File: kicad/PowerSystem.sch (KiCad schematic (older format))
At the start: 15 parts, among them U201 LF120ABDT-TR, U202 TPS70933

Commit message: Started assigning foot prints to the parts
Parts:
- removed W201: TEST_1P, symbol TEST_1P
- C201: footprint (none) -> Capacitors_SMD:C_0805
- C202: value 1μF 50V -> 1μF 25V; footprint (none) -> Capacitors_SMD:C_1210; Conrad-PN (none) -> Value; Digikey-PN (none) -> Value; MFP (none) -> Value
- C203: value 02.2μF 50V -> 2.2μF 50V; footprint (none) -> Capacitors_SMD:C_1210; Conrad-PN (none) -> N/A; Digikey-PN (none) -> 1276-2884-1-ND; MFP (none) -> CL32B225KBJNNNE
- C204: footprint (none) -> Capacitors_SMD:C_1210; Conrad-PN (none) -> Value; Digikey-PN (none) -> Value; MFP (none) -> Value
- D201: value LED -> 12VDC; footprint (none) -> LEDs:LED_0805
- D202: value LED -> 3V3DC; footprint (none) -> LEDs:LED_0805
- R201, R202, R203, R204: footprint (none) -> Resistors_SMD:R_0805
- TP201, TP202: footprint (none) -> Measurement_Points:Measurement_Point_Round-SMD-Pad_Small
- U201: Conrad-PN (none) -> 1185937 - 62; Digikey-PN (none) -> 497-8330-1-ND
- U202: Conrad-PN (none) -> 1261694 - 62; Digikey-PN (none) -> 296-35483-1-ND
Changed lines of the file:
@@
 F 0 "R202" V 3280 3850 50  0000 C CNN
 F 1 "0Ω" V 3200 3850 50  0000 C CNN
-F 2 "" V 3130 3850 50  0000 C CNN
+F 2 "Resistors_SMD:R_0805" V 3130 3850 50  0001 C CNN
 F 3 "" H 3200 3850 50  0000 C CNN
 	1    3200 3850
@@
 U+
 $Comp
-L GND #PWR202
+L GND #PWR011
 U 1 1 584DB061
 P 3900 4450
-F 0 "#PWR202" H 3900 4200 50  0001 C CNN
+F 0 "#PWR011" H 3900 4200 50  0001 C CNN
 F 1 "GND" H 3900 4300 50  0000 C CNN
 F 2 "" H 3900 4450 50  0000 C CNN
@@
 P 2600 4050
 F 0 "C202" H 2625 4150 50  0000 L CNN
-F 1 "1μF 50V" H 2625 3950 50  0000 L CNN
-F 2 "" H 2638 3900 50  0000 C CNN
+F 1 "1μF 25V" H 2625 3950 50  0000 L CNN
+F 2 "Capacitors_SMD:C_1210" H 2638 3900 50  0001 C CNN
 F 3 "" H 2600 4050 50  0000 C CNN
+F 4 "Value" H 2600 4050 60  0001 C CNN "MFP"
+F 5 "Value" H 2600 4050 60  0001 C CNN "Conrad-PN"
+F 6 "Value" H 2600 4050 60  0001 C CNN "Digikey-PN"
 	1    2600 4050
 	1    0    0    -1
@@
 F 0 "C204" H 4675 4150 50  0000 L CNN
 F 1 "1μF 16V" H 4675 3950 50  0000 L CNN
-F 2 "" H 4688 3900 50  0000 C CNN
+F 2 "Capacitors_SMD:C_1210" H 4688 3900 50  0001 C CNN
 F 3 "" H 4650 4050 50  0000 C CNN
+F 4 "Value" H 4650 4050 60  0001 C CNN "MFP"
+F 5 "Value" H 4650 4050 60  0001 C CNN "Conrad-PN"
+F 6 "Value" H 4650 4050 60  0001 C CNN "Digikey-PN"
 	1    4650 4050
 	1    0    0    -1
@@
 P 5250 4050
 F 0 "D202" H 5250 4150 50  0000 C CNN
-F 1 "LED" H 5250 3950 50  0000 C CNN
-F 2 "" H 5250 4050 50  0000 C CNN
+F 1 "3V3DC" H 5250 3950 50  0000 C CNN
+F 2 "LEDs:LED_0805" H 5250 4050 50  0001 C CNN
 F 3 "" H 5250 4050 50  0000 C CNN
 	1    5250 4050
@@
 F 0 "R204" V 5330 4550 50  0000 C CNN
 F 1 "660Ω" V 5250 4550 50  0000 C CNN
-F 2 "" V 5180 4550 50  0000 C CNN
+F 2 "Resistors_SMD:R_0805" V 5180 4550 50  0001 C CNN
 F 3 "" H 5250 4550 50  0000 C CNN
 	1    5250 4550
@@
 $EndComp
 $Comp
-L GND #PWR204
+L GND #PWR012
 U 1 1 584DB084
 P 5250 4900
-F 0 "#PWR204" H 5250 4650 50  0001 C CNN
+F 0 "#PWR012" H 5250 4650 50  0001 C CNN
 F 1 "GND" H 5250 4750 50  0000 C CNN
 F 2 "" H 5250 4900 50  0000 C CNN
 F 3 "" H 5250 4900 50  0000 C CNN
 	1    5250 4900
-	1    0    0    -1
-$EndComp
-$Comp
-L TEST_1P W201
-U 1 1 584DB091
-P 2500 3500
-F 0 "W201" H 2500 3770 50  0000 C CNN
-F 1 "TEST_1P" H 2500 3700 50  0000 C CNN
-F 2 "" H 2700 3500 50  0000 C CNN
-F 3 "" H 2700 3500 50  0000 C CNN
-	1    2500 3500
 	1    0    0    -1
 $EndComp
@@
 F 0 "U202" H 4150 3350 60  0000 C CNN
 F 1 "TPS70933" H 3900 3700 60  0000 C CNN
-F 2 "" H 3750 3700 60  0000 C CNN
+F 2 "" H 3750 3700 60  0001 C CNN
 F 3 "" H 3750 3700 60  0000 C CNN
 F 4 "TPS70933DBVR" H 3900 3700 60  0001 C CNN "MFP"
+F 5 "1261694 - 62" H 3900 3700 60  0001 C CNN "Conrad-PN"
+F 6 "296-35483-1-ND" H 3900 3700 60  0001 C CNN "Digikey-PN"
 	1    3900 3700
 	1    0    0    -1
@@
 F 0 "U201" H 4150 1200 60  0000 C CNN
 F 1 "LF120ABDT-TR" H 3900 1550 60  0000 C CNN
-F 2 "" H 3750 1550 60  0000 C CNN
+F 2 "" H 3750 1550 60  0001 C CNN
 F 3 "" H 3750 1550 60  0000 C CNN
 F 4 "LF120ABDT-TR" H 3900 1550 60  0001 C CNN "MFP"
+F 5 "1185937 - 62" H 3900 1550 60  0001 C CNN "Conrad-PN"
+F 6 "497-8330-1-ND" H 3900 1550 60  0001 C CNN "Digikey-PN"
 	1    3900 1550
 	1    0    0    -1
@@
 	5400 3500 5400 3550
 Connection ~ 5400 3550
-Wire Wire Line
-	2500 3500 2500 3550
-Connection ~ 2500 3550
 Text HLabel 5850 3550 2    60   Input ~ 0
 UbOut
@@
 F 0 "C201" H 2575 1950 50  0000 L CNN
 F 1 "0.1μF 50V" H 2575 1750 50  0000 L CNN
-F 2 "" H 2588 1700 50  0000 C CNN
+F 2 "Capacitors_SMD:C_0805" H 2588 1700 50  0001 C CNN
 F 3 "" H 2550 1850 50  0000 C CNN
 	1    2550 1850
@@
 P 4600 1850
 F 0 "C203" H 4625 1950 50  0000 L CNN
-F 1 "02.2μF 50V" H 4625 1750 50  0000 L CNN
-F 2 "" H 4638 1700 50  0000 C CNN
+F 1 "2.2μF 50V" H 4625 1750 50  0000 L CNN
+F 2 "Capacitors_SMD:C_1210" H 4638 1700 50  0001 C CNN
 F 3 "" H 4600 1850 50  0000 C CNN
+F 4 "CL32B225KBJNNNE" H 4600 1850 60  0001 C CNN "MFP"
+F 5 "N/A" H 4600 1850 60  0001 C CNN "Conrad-PN"
+F 6 "1276-2884-1-ND" H 4600 1850 60  0001 C CNN "Digikey-PN"
 	1    4600 1850
 	1    0    0    -1
 $EndComp
 $Comp
-L GND #PWR201
+L GND #PWR013
 U 1 1 584DD17A
 P 3900 2650
-F 0 "#PWR201" H 3900 2400 50  0001 C CNN
+F 0 "#PWR013" H 3900 2400 50  0001 C CNN
 F 1 "GND" H 3900 2500 50  0000 C CNN
 F 2 "" H 3900 2650 50  0000 C CNN
@@
 F 0 "R201" V 3280 2050 50  0000 C CNN
 F 1 "0Ω" V 3200 2050 50  0000 C CNN
-F 2 "" V 3130 2050 50  0000 C CNN
+F 2 "Resistors_SMD:R_0805" V 3130 2050 50  0001 C CNN
 F 3 "" H 3200 2050 50  0000 C CNN
 F 4 "VALUE" H 3200 2050 60  0001 C CNN "MFP"
@@
 P 5250 1850
 F 0 "D201" H 5250 1950 50  0000 C CNN
-F 1 "LED" H 5250 1750 50  0000 C CNN
-F 2 "" H 5250 1850 50  0000 C CNN
+F 1 "12VDC" H 5250 1750 50  0000 C CNN
+F 2 "LEDs:LED_0805" H 5250 1850 50  0001 C CNN
 F 3 "" H 5250 1850 50  0000 C CNN
 	1    5250 1850
@@
 F 0 "R203" V 5330 2350 50  0000 C CNN
 F 1 "2k4Ω" V 5250 2350 50  0000 C CNN
-F 2 "" V 5180 2350 50  0000 C CNN
+F 2 "Resistors_SMD:R_0805" V 5180 2350 50  0001 C CNN
 F 3 "" H 5250 2350 50  0000 C CNN
 	1    5250 2350
@@
 $EndComp
 $Comp
-L GND #PWR203
+L GND #PWR014
 U 1 1 584DD971
 P 5250 2650
-F 0 "#PWR203" H 5250 2400 50  0001 C CNN
+F 0 "#PWR014" H 5250 2400 50  0001 C CNN
 F 1 "GND" H 5250 2500 50  0000 C CNN
 F 2 "" H 5250 2650 50  0000 C CNN
@@
 F 0 "TP202" H 5600 1470 50  0000 C CNN
 F 1 "TP12V" H 5600 1400 50  0000 C CNN
-F 2 "" H 5800 1200 50  0000 C CNN
+F 2 "Measurement_Points:Measurement_Point_Round-SMD-Pad_Small" H 5800 1200 50  0001 C CNN
 F 3 "" H 5800 1200 50  0000 C CNN
 	1    5600 1200
@@
 F 0 "TP201" H 5400 3770 50  0000 C CNN
 F 1 "TP3V3" H 5400 3700 50  0000 C CNN
-F 2 "" H 5600 3500 50  0000 C CNN
+F 2 "Measurement_Points:Measurement_Point_Round-SMD-Pad_Small" H 5600 3500 50  0001 C CNN
 F 3 "" H 5600 3500 50  0000 C CNN
 	1    5400 3500

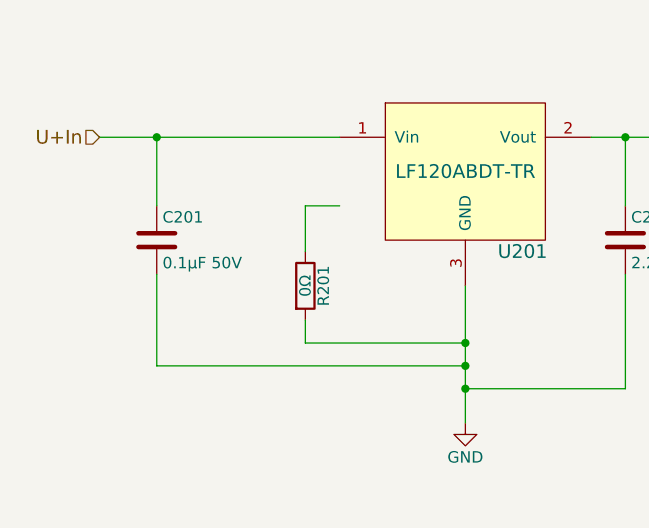
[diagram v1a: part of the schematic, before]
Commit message: Added more footprints to the parts
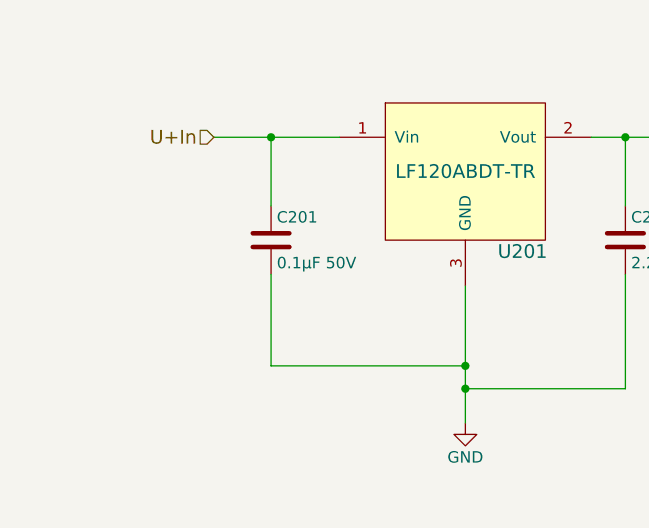
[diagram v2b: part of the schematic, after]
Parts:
- removed R201: 0Ω, Resistors_SMD:R_0805, symbol R
- U201: footprint (none) -> tl2c-footprint:LF120ABDT-TR
- U202: footprint (none) -> tl2c-footprint:TPS70933DBVR
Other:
- moved on the sheet: C201
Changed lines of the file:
@@
 F 0 "U202" H 4150 3350 60  0000 C CNN
 F 1 "TPS70933" H 3900 3700 60  0000 C CNN
-F 2 "" H 3750 3700 60  0001 C CNN
+F 2 "tl2c-footprint:TPS70933DBVR" H 3750 3700 60  0001 C CNN
 F 3 "" H 3750 3700 60  0000 C CNN
 F 4 "TPS70933DBVR" H 3900 3700 60  0001 C CNN "MFP"
@@
 F 0 "U201" H 4150 1200 60  0000 C CNN
 F 1 "LF120ABDT-TR" H 3900 1550 60  0000 C CNN
-F 2 "" H 3750 1550 60  0001 C CNN
+F 2 "tl2c-footprint:LF120ABDT-TR" H 3750 1550 60  0001 C CNN
 F 3 "" H 3750 1550 60  0000 C CNN
 F 4 "LF120ABDT-TR" H 3900 1550 60  0001 C CNN "MFP"
@@
 	4450 1400 6150 1400
 Wire Wire Line
-	2300 1400 3350 1400
+	2800 1400 3350 1400
 $Comp
 L C C201
 U 1 1 584DCFF9
-P 2550 1850
-F 0 "C201" H 2575 1950 50  0000 L CNN
-F 1 "0.1μF 50V" H 2575 1750 50  0000 L CNN
-F 2 "Capacitors_SMD:C_0805" H 2588 1700 50  0001 C CNN
-F 3 "" H 2550 1850 50  0000 C CNN
-	1    2550 1850
+P 3050 1850
+F 0 "C201" H 3075 1950 50  0000 L CNN
+F 1 "0.1μF 50V" H 3075 1750 50  0000 L CNN
+F 2 "Capacitors_SMD:C_0805" H 3088 1700 50  0001 C CNN
+F 3 "" H 3050 1850 50  0000 C CNN
+	1    3050 1850
 	1    0    0    -1
 $EndComp
@@
 Text HLabel 6150 1400 2    60   Input ~ 0
 U+Out
-Text HLabel 2300 1400 0    60   Input ~ 0
+Text HLabel 2800 1400 0    60   Input ~ 0
 U+In
 Wire Wire Line
 	3900 2050 3900 2650
-$Comp
-L R R201
-U 1 1 584DD244
-P 3200 2050
-F 0 "R201" V 3280 2050 50  0000 C CNN
-F 1 "0Ω" V 3200 2050 50  0000 C CNN
-F 2 "Resistors_SMD:R_0805" V 3130 2050 50  0001 C CNN
-F 3 "" H 3200 2050 50  0000 C CNN
-F 4 "VALUE" H 3200 2050 60  0001 C CNN "MFP"
-	1    3200 2050
-	1    0    0    -1
-$EndComp
 Wire Wire Line
-	3350 1700 3200 1700
+	3050 1400 3050 1700
+Connection ~ 3050 1400
 Wire Wire Line
-	3200 1700 3200 1900
+	3050 2000 3050 2400
 Wire Wire Line
-	3200 2200 3200 2300
-Wire Wire Line
-	3200 2300 3900 2300
-Connection ~ 3900 2300
-Wire Wire Line
-	2550 1400 2550 1700
-Connection ~ 2550 1400
-Wire Wire Line
-	2550 2000 2550 2400
-Wire Wire Line
-	2550 2400 3900 2400
+	3050 2400 3900 2400
 Connection ~ 3900 2400
 Wire Wire Line

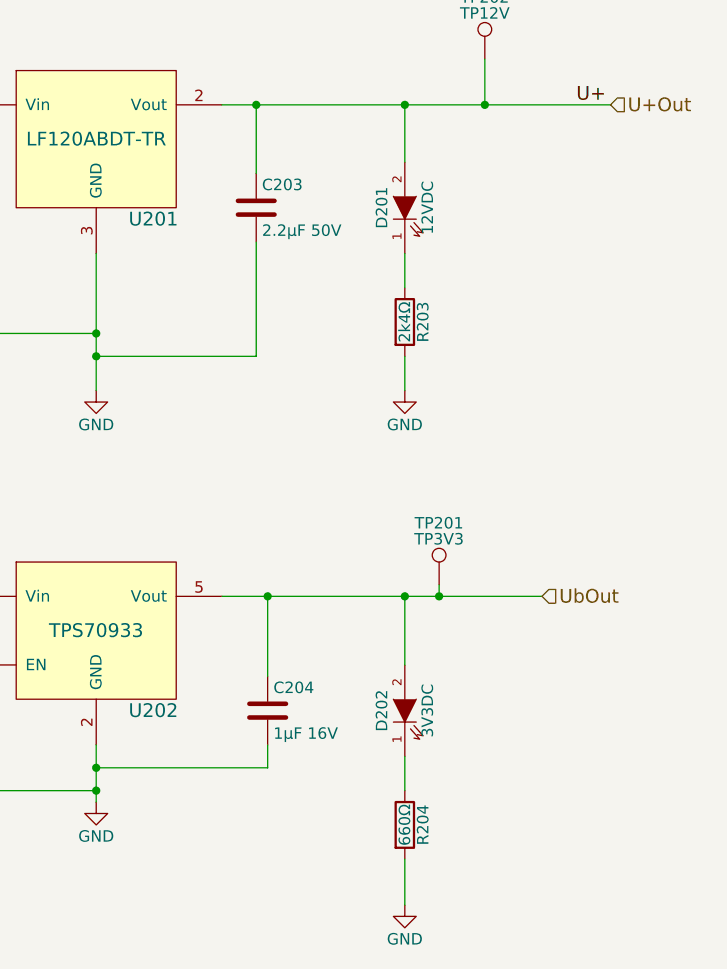
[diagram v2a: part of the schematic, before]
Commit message: Started adding tracks to the layout
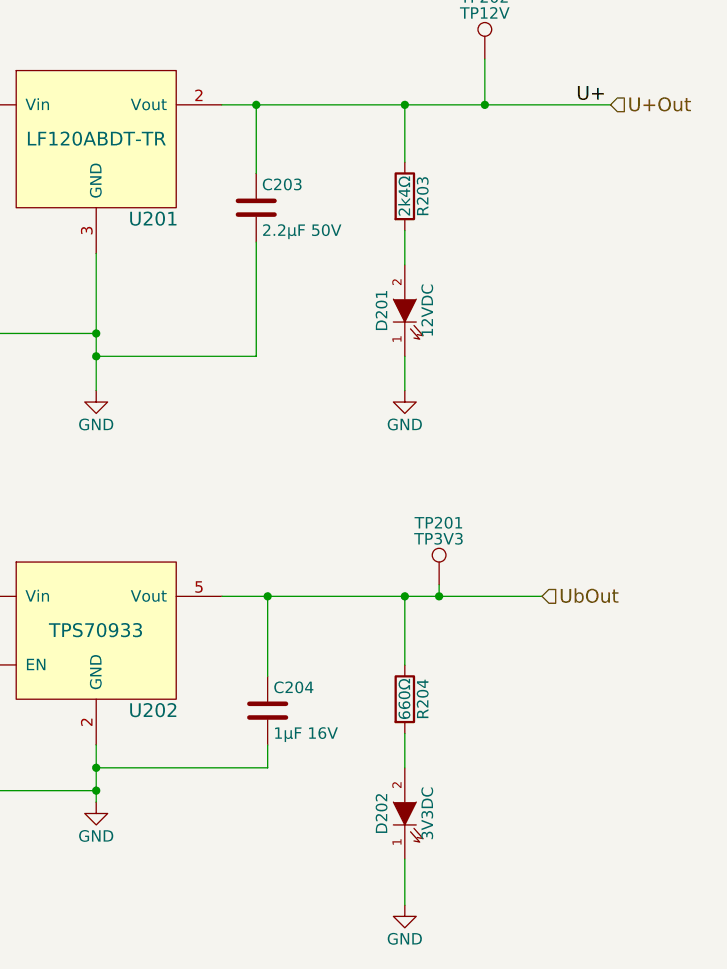
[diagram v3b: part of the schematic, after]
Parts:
- TP202: footprint Measurement_Points:Measurement_Point_Round-SMD-Pad_Small -> Pin_Headers:Pin_Header_Straight_1x01; Conrad-PN (none) -> Value; Digikey-PN (none) -> Value; MFP (none) -> Value
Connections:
- net GND: now also D201.1 (K), D202.1 (K); no longer R203.2, R204.2
- net U+Out: now also R203.1; no longer D201.2 (A)
- net UbOut: now also R204.1; no longer D202.2 (A)
- new net: D202.2 (A), R204.2
- new net: D201.2 (A), R203.2
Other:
- moved on the sheet: D201, D202, R203, R204
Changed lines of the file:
@@
 U+
 $Comp
-L GND #PWR011
+L GND #PWR014
 U 1 1 584DB061
 P 3900 4450
-F 0 "#PWR011" H 3900 4200 50  0001 C CNN
+F 0 "#PWR014" H 3900 4200 50  0001 C CNN
 F 1 "GND" H 3900 4300 50  0000 C CNN
 F 2 "" H 3900 4450 50  0000 C CNN
@@
 L LED D202
 U 1 1 584DB076
-P 5250 4050
-F 0 "D202" H 5250 4150 50  0000 C CNN
-F 1 "3V3DC" H 5250 3950 50  0000 C CNN
-F 2 "LEDs:LED_0805" H 5250 4050 50  0001 C CNN
-F 3 "" H 5250 4050 50  0000 C CNN
-	1    5250 4050
+P 5250 4500
+F 0 "D202" H 5250 4600 50  0000 C CNN
+F 1 "3V3DC" H 5250 4400 50  0000 C CNN
+F 2 "LEDs:LED_0805" H 5250 4500 50  0001 C CNN
+F 3 "" H 5250 4500 50  0000 C CNN
+	1    5250 4500
 	0    -1   -1   0
 $EndComp
@@
 L R R204
 U 1 1 584DB07D
-P 5250 4550
-F 0 "R204" V 5330 4550 50  0000 C CNN
-F 1 "660Ω" V 5250 4550 50  0000 C CNN
-F 2 "Resistors_SMD:R_0805" V 5180 4550 50  0001 C CNN
-F 3 "" H 5250 4550 50  0000 C CNN
-	1    5250 4550
-	1    0    0    -1
-$EndComp
-$Comp
-L GND #PWR012
+P 5250 4000
+F 0 "R204" V 5330 4000 50  0000 C CNN
+F 1 "660Ω" V 5250 4000 50  0000 C CNN
+F 2 "Resistors_SMD:R_0805" V 5180 4000 50  0001 C CNN
+F 3 "" H 5250 4000 50  0000 C CNN
+	1    5250 4000
+	1    0    0    -1
+$EndComp
+$Comp
+L GND #PWR015
 U 1 1 584DB084
 P 5250 4900
-F 0 "#PWR012" H 5250 4650 50  0001 C CNN
+F 0 "#PWR015" H 5250 4650 50  0001 C CNN
 F 1 "GND" H 5250 4750 50  0000 C CNN
 F 2 "" H 5250 4900 50  0000 C CNN
@@
 Connection ~ 5250 3550
 Wire Wire Line
-	5250 4250 5250 4400
-Wire Wire Line
 	5250 4700 5250 4900
 Wire Wire Line
@@
 $EndComp
 $Comp
-L GND #PWR013
+L GND #PWR016
 U 1 1 584DD17A
 P 3900 2650
-F 0 "#PWR013" H 3900 2400 50  0001 C CNN
+F 0 "#PWR016" H 3900 2400 50  0001 C CNN
 F 1 "GND" H 3900 2500 50  0000 C CNN
 F 2 "" H 3900 2650 50  0000 C CNN
@@
 L LED D201
 U 1 1 584DD7AB
-P 5250 1850
-F 0 "D201" H 5250 1950 50  0000 C CNN
-F 1 "12VDC" H 5250 1750 50  0000 C CNN
-F 2 "LEDs:LED_0805" H 5250 1850 50  0001 C CNN
-F 3 "" H 5250 1850 50  0000 C CNN
-	1    5250 1850
+P 5250 2300
+F 0 "D201" H 5250 2400 50  0000 C CNN
+F 1 "12VDC" H 5250 2200 50  0000 C CNN
+F 2 "LEDs:LED_0805" H 5250 2300 50  0001 C CNN
+F 3 "" H 5250 2300 50  0000 C CNN
+	1    5250 2300
 	0    -1   -1   0
 $EndComp
@@
 L R R203
 U 1 1 584DD8C0
-P 5250 2350
-F 0 "R203" V 5330 2350 50  0000 C CNN
-F 1 "2k4Ω" V 5250 2350 50  0000 C CNN
-F 2 "Resistors_SMD:R_0805" V 5180 2350 50  0001 C CNN
-F 3 "" H 5250 2350 50  0000 C CNN
-	1    5250 2350
-	1    0    0    -1
-$EndComp
-$Comp
-L GND #PWR014
+P 5250 1800
+F 0 "R203" V 5330 1800 50  0000 C CNN
+F 1 "2k4Ω" V 5250 1800 50  0000 C CNN
+F 2 "Resistors_SMD:R_0805" V 5180 1800 50  0001 C CNN
+F 3 "" H 5250 1800 50  0000 C CNN
+	1    5250 1800
+	1    0    0    -1
+$EndComp
+$Comp
+L GND #PWR017
 U 1 1 584DD971
 P 5250 2650
-F 0 "#PWR014" H 5250 2400 50  0001 C CNN
+F 0 "#PWR017" H 5250 2400 50  0001 C CNN
 F 1 "GND" H 5250 2500 50  0000 C CNN
 F 2 "" H 5250 2650 50  0000 C CNN
@@
 	1    0    0    -1
 $EndComp
-Wire Wire Line
-	5250 2050 5250 2200
 Wire Wire Line
 	5250 2500 5250 2650
@@
 F 0 "TP202" H 5600 1470 50  0000 C CNN
 F 1 "TP12V" H 5600 1400 50  0000 C CNN
-F 2 "Measurement_Points:Measurement_Point_Round-SMD-Pad_Small" H 5800 1200 50  0001 C CNN
+F 2 "Pin_Headers:Pin_Header_Straight_1x01" H 5800 1200 50  0001 C CNN
 F 3 "" H 5800 1200 50  0000 C CNN
+F 4 "Value" H 5600 1200 60  0001 C CNN "MFP"
+F 5 "Value" H 5600 1200 60  0001 C CNN "Conrad-PN"
+F 6 "Value" H 5600 1200 60  0001 C CNN "Digikey-PN"
 	1    5600 1200
 	1    0    0    -1
@@
 	1    0    0    -1
 $EndComp
+Wire Wire Line
+	5250 2100 5250 1950
+Wire Wire Line
+	5250 4150 5250 4300
 $EndSCHEMATC

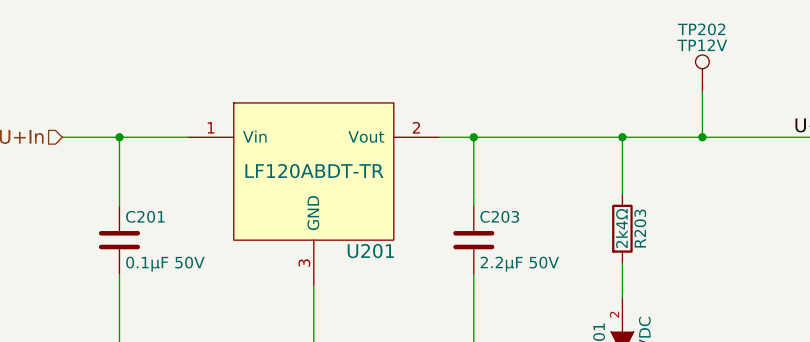
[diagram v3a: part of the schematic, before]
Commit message: A change of heart with some of the parts due to sourcing
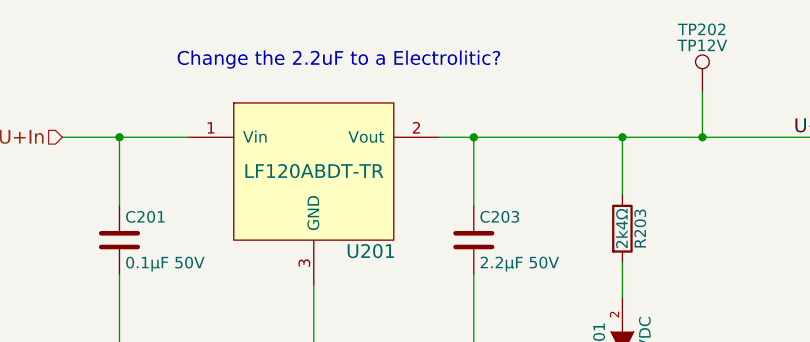
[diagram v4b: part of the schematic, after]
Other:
- note added: "Change the 2.2uF to a Electrolitic?"
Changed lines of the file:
@@
 Wire Wire Line
 	5250 4150 5250 4300
+Text Notes 3300 1100 0    60   ~ 0
+Change the 2.2uF to a Electrolitic?
 $EndSCHEMATC

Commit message: Some part changes due to sourcing
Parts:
- C203: footprint Capacitors_SMD:C_1210 -> Capacitors_SMD:C_1206; Conrad-PN N/A -> 450955 - 62; Digikey-PN 1276-2884-1-ND -> N/A
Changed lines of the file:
@@
 F 0 "C203" H 4625 1950 50  0000 L CNN
 F 1 "2.2μF 50V" H 4625 1750 50  0000 L CNN
-F 2 "Capacitors_SMD:C_1210" H 4638 1700 50  0001 C CNN
+F 2 "Capacitors_SMD:C_1206" H 4638 1700 50  0001 C CNN
 F 3 "" H 4600 1850 50  0000 C CNN
 F 4 "CL32B225KBJNNNE" H 4600 1850 60  0001 C CNN "MFP"
-F 5 "N/A" H 4600 1850 60  0001 C CNN "Conrad-PN"
-F 6 "1276-2884-1-ND" H 4600 1850 60  0001 C CNN "Digikey-PN"
+F 5 "450955 - 62" H 4600 1850 60  0001 C CNN "Conrad-PN"
+F 6 "N/A" H 4600 1850 60  0001 C CNN "Digikey-PN"
 	1    4600 1850
 	1    0    0    -1
